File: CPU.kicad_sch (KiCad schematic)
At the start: 53 parts, among them Y1 X322524MKB4SI

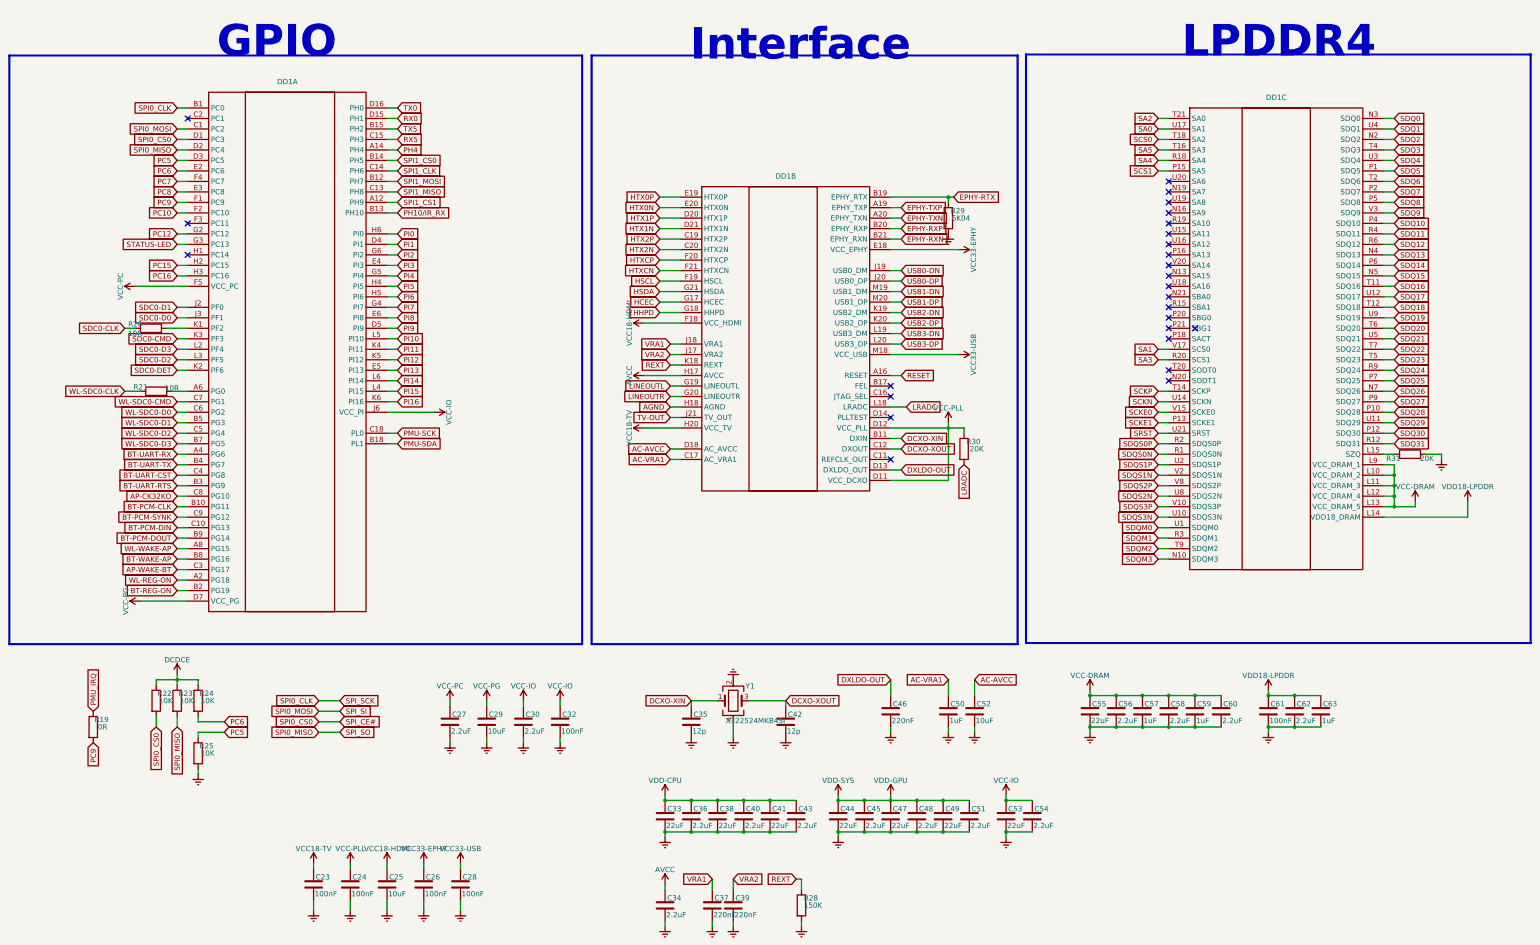
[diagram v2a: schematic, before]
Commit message: Исправление УГО по ГОСТу, добавление 3D моделей
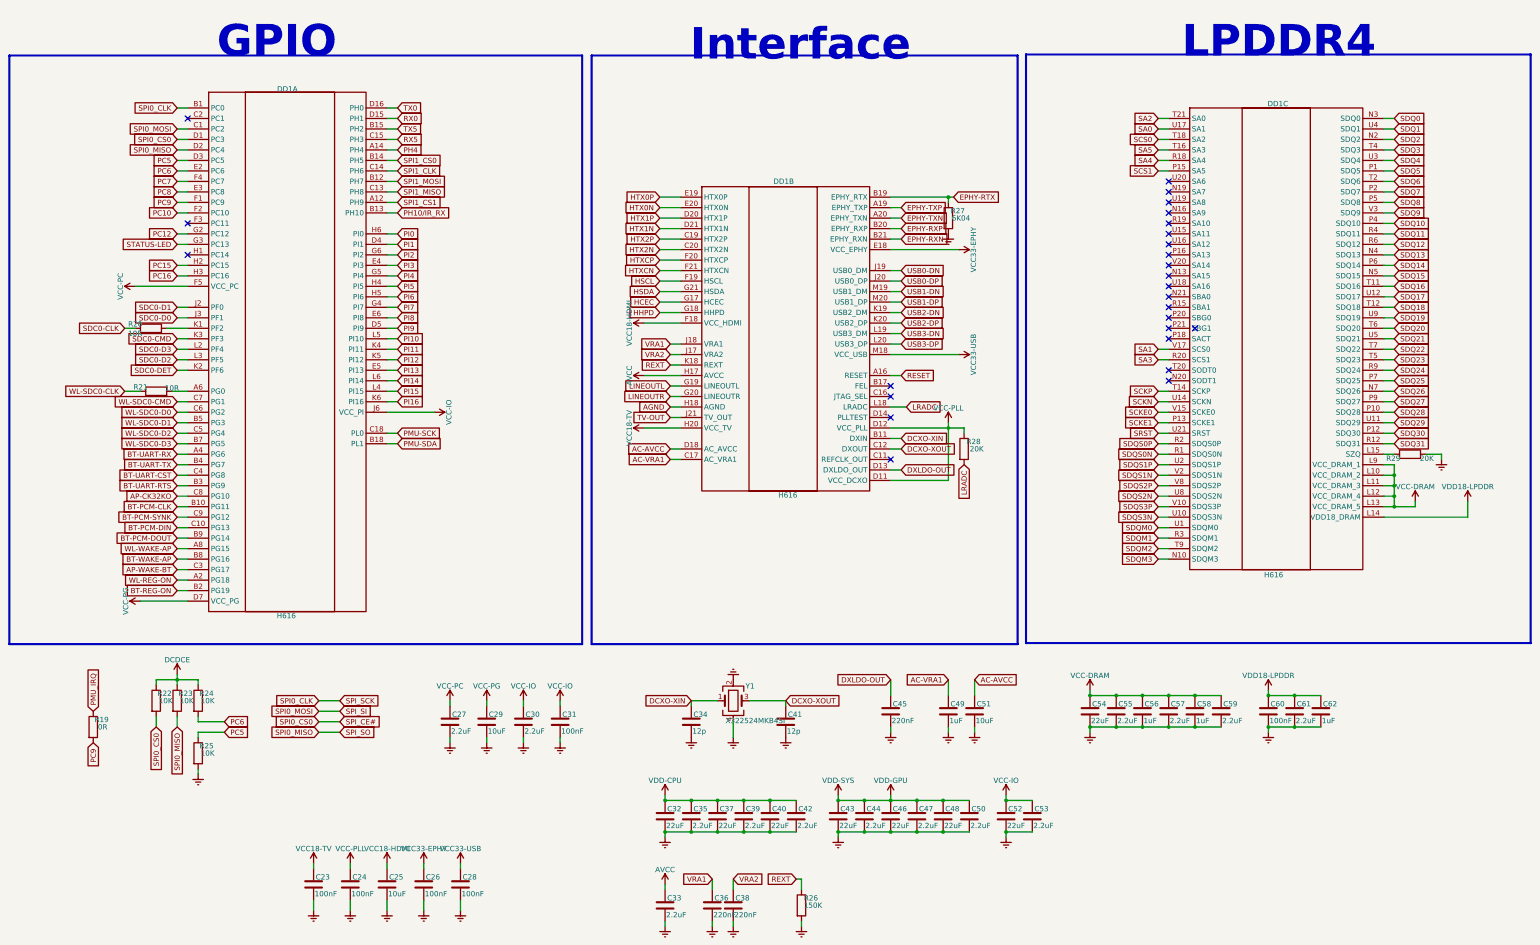
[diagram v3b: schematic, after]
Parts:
- DD1: value ~ -> H616
- renumbered C32 to C31, C33 to C32, C34 to C33, C35 to C34, C36 to C35, C37 to C36, C38 to C37, C39 to C38, C40 to C39, C41 to C40, C42 to C41, C43 to C42, C44 to C43, C45 to C44, C46 to C45, C47 to C46, C48 to C47, C49 to C48, C50 to C49, C51 to C50, C52 to C51, C53 to C52, C54 to C53, C55 to C54, C56 to C55, C57 to C56, C58 to C57, C59 to C58, C60 to C59, C61 to C60, C62 to C61, C63 to C62, R28 to R26, R29 to R27, R30 to R28, R31 to R29
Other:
- company: @madjogger -> РТУ МИРЭА
